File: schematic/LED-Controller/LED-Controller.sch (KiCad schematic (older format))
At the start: 16 parts, among them J1 5V Power, J10 String6, J2 ICSP, J3 RCin, J4 Serial Connect, J5 String1, J6 String2, J7 String3, J8 String4, J9 String5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

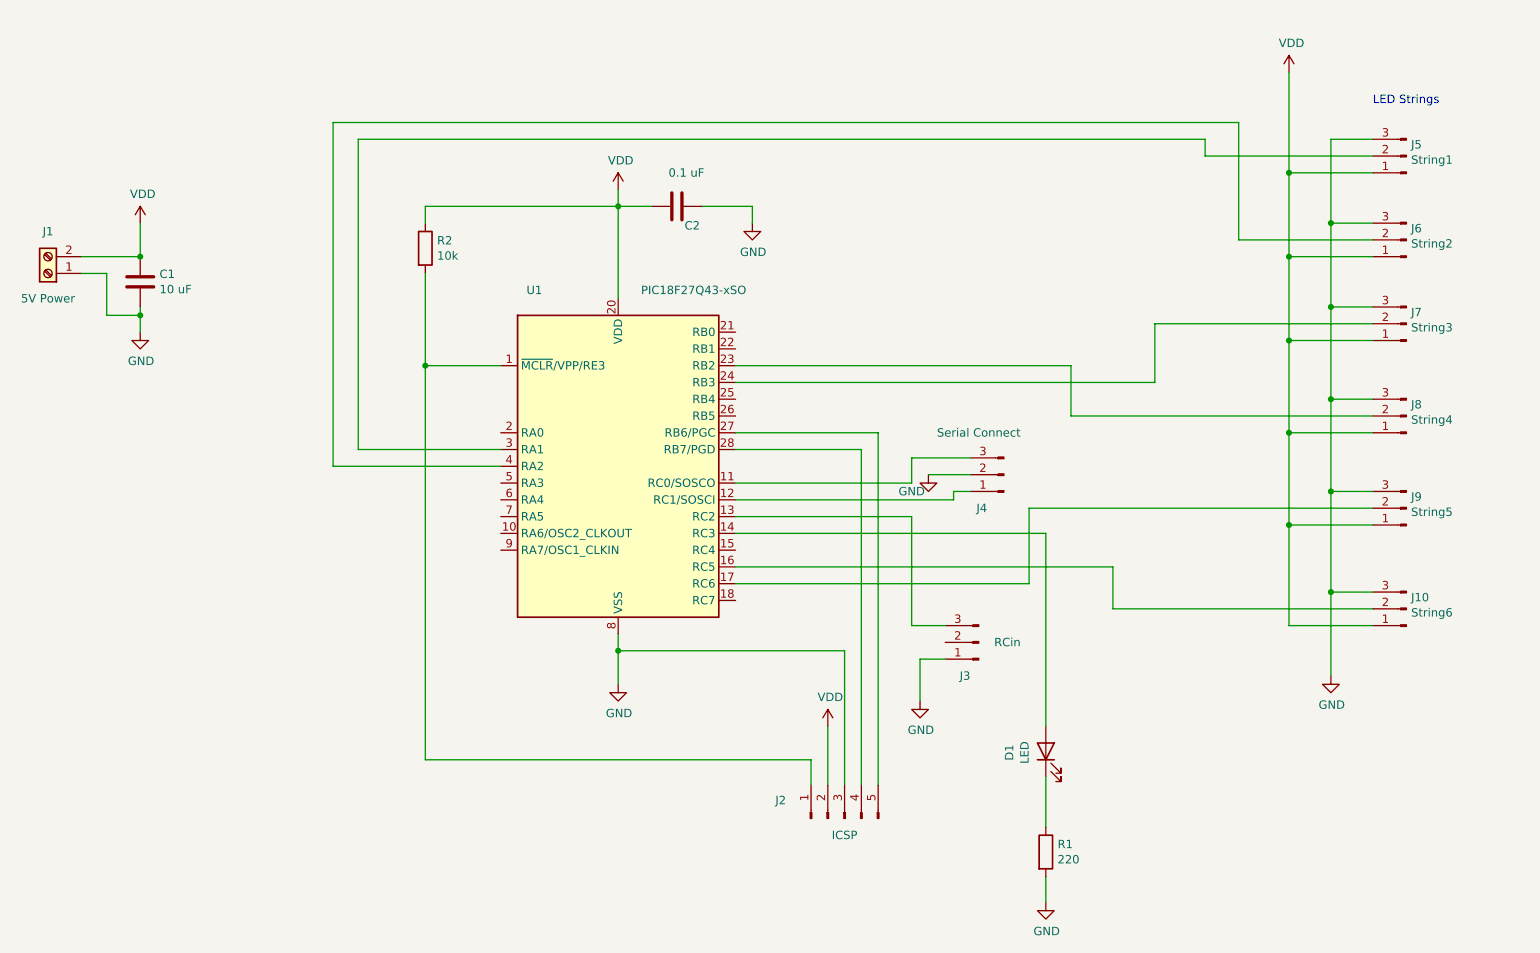
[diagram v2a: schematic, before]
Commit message: Added flexible power for uController
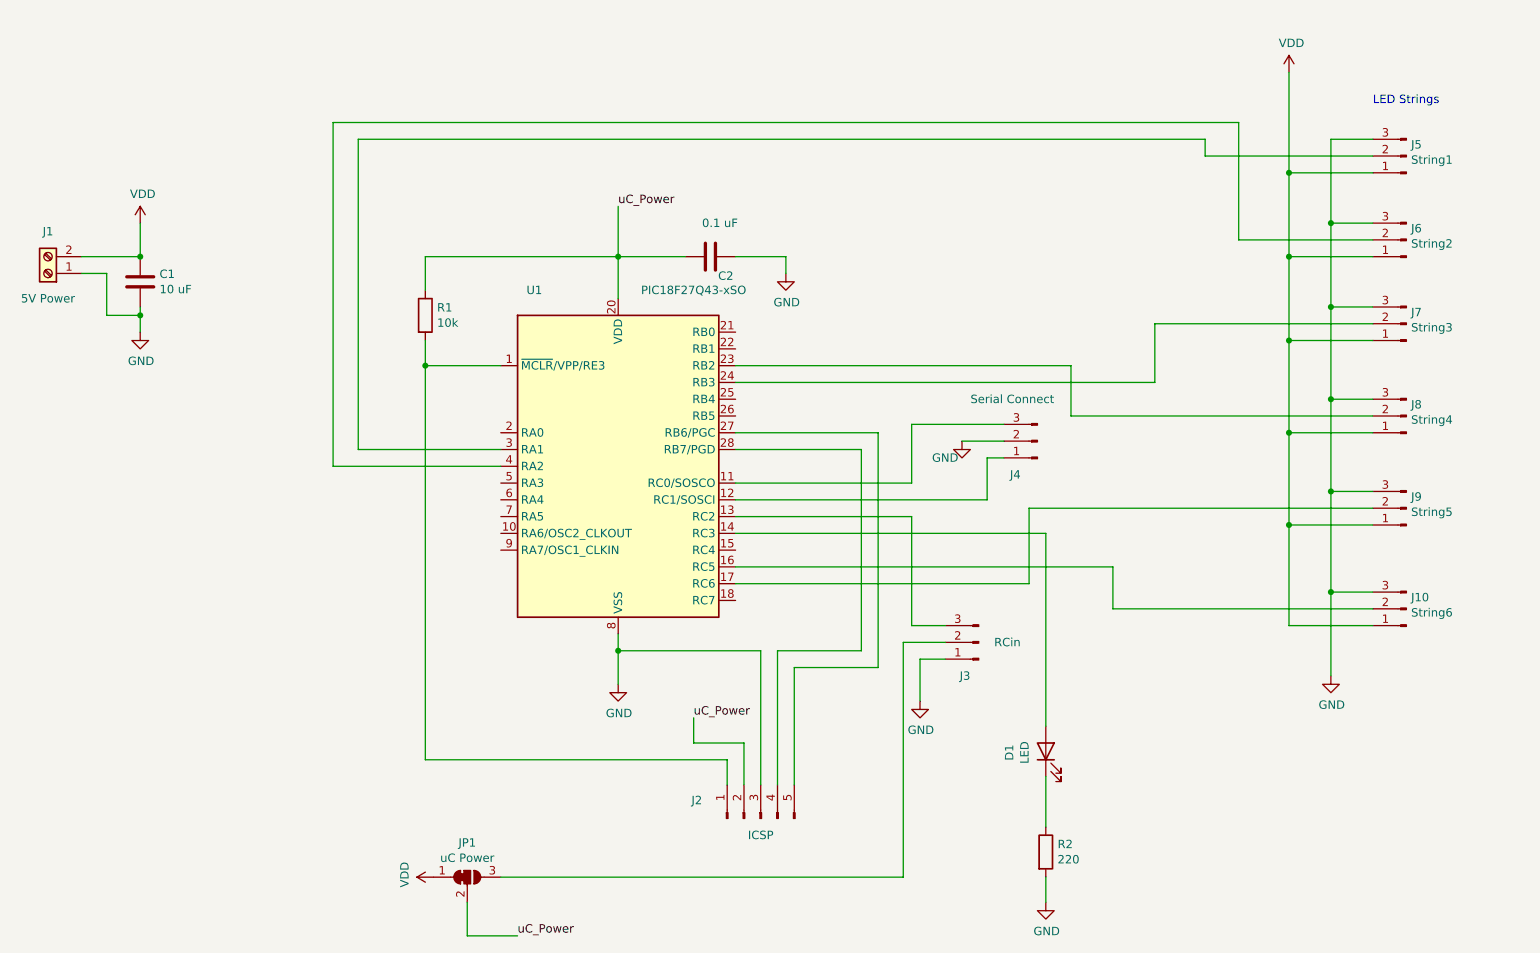
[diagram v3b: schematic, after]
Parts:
- added JP1: uC Power, symbol Jumper:SolderJumper_3_Bridged12
- renumbered R2 to R1, R1 to R2
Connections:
- net VDD: now also JP1.1 (A); no longer C2.2, J2.2 (Pin_2), R1.1, U1.20 (VDD)
- net at J3.2 (Pin_2): now also JP1.3 (B)
- new net uC_Power: C2.2, J2.2 (Pin_2), JP1.2 (C), R1.1, U1.20 (VDD)
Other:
- moved on the sheet: C2, J2, J4, R1
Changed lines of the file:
@@
 L Connector:Conn_01x03_Male J4
 U 1 1 602A7478
-P 6750 3600
-F 0 "J4" H 6850 3800 50  0000 L CNN
-F 1 "Serial Connect" H 6650 3350 50  0000 L CNN
-F 2 "Connector_PinHeader_2.54mm:PinHeader_1x03_P2.54mm_Vertical" H 6750 3600 50  0001 C CNN
-F 3 "~" H 6750 3600 50  0001 C CNN
-	1    6750 3600
+P 6950 3400
+F 0 "J4" H 7050 3600 50  0000 L CNN
+F 1 "Serial Connect" H 6850 3150 50  0000 L CNN
+F 2 "Connector_PinHeader_2.54mm:PinHeader_1x03_P2.54mm_Vertical" H 6950 3400 50  0001 C CNN
+F 3 "~" H 6950 3400 50  0001 C CNN
+	1    6950 3400
 	-1   0    0    1
 $EndComp
@@
 L Device:C C2
 U 1 1 602AFB39
-P 4800 2000
-F 0 "C2" V 4915 2046 50  0000 L CNN
-F 1 "0.1 uF" V 4600 1950 50  0000 L CNN
-F 2 "Capacitor_SMD:C_0603_1608Metric_Pad1.08x0.95mm_HandSolder" H 4838 1850 50  0001 C CNN
-F 3 "~" H 4800 2000 50  0001 C CNN
-	1    4800 2000
+P 5000 2300
+F 0 "C2" V 5115 2346 50  0000 L CNN
+F 1 "0.1 uF" V 4800 2250 50  0000 L CNN
+F 2 "Capacitor_SMD:C_0603_1608Metric_Pad1.08x0.95mm_HandSolder" H 5038 2150 50  0001 C CNN
+F 3 "~" H 5000 2300 50  0001 C CNN
+	1    5000 2300
 	0    1    1    0
 $EndComp
@@
 $EndComp
 $Comp
-L power:GND #PWR06
+L power:GND #PWR05
 U 1 1 602B1183
-P 5250 2100
-F 0 "#PWR06" H 5250 1850 50  0001 C CNN
-F 1 "GND" H 5255 1927 50  0000 C CNN
-F 2 "" H 5250 2100 50  0001 C CNN
-F 3 "" H 5250 2100 50  0001 C CNN
-	1    5250 2100
+P 5450 2400
+F 0 "#PWR05" H 5450 2150 50  0001 C CNN
+F 1 "GND" H 5455 2227 50  0000 C CNN
+F 2 "" H 5450 2400 50  0001 C CNN
+F 3 "" H 5450 2400 50  0001 C CNN
+	1    5450 2400
 	1    0    0    -1
 $EndComp
@@
 $EndComp
 $Comp
-L power:VDD #PWR010
+L power:VDD #PWR09
 U 1 1 602C05A1
 P 8450 1200
-F 0 "#PWR010" H 8450 1050 50  0001 C CNN
+F 0 "#PWR09" H 8450 1050 50  0001 C CNN
 F 1 "VDD" H 8465 1373 50  0000 C CNN
 F 2 "" H 8450 1200 50  0001 C CNN
@@
 $EndComp
 $Comp
-L power:GND #PWR011
+L power:GND #PWR010
 U 1 1 602C0B28
 P 8700 4800
-F 0 "#PWR011" H 8700 4550 50  0001 C CNN
+F 0 "#PWR010" H 8700 4550 50  0001 C CNN
 F 1 "GND" H 8705 4627 50  0000 C CNN
 F 2 "" H 8700 4800 50  0001 C CNN
@@
 L Connector:Conn_01x05_Male J2
 U 1 1 602D318D
-P 5800 5650
-F 0 "J2" V 5908 6031 50  0000 C CNN
-F 1 "ICSP" V 5700 5650 50  0000 C CNN
-F 2 "Connector_PinHeader_2.54mm:PinHeader_1x05_P2.54mm_Vertical" H 5800 5650 50  0001 C CNN
-F 3 "~" H 5800 5650 50  0001 C CNN
-	1    5800 5650
+P 5300 5650
+F 0 "J2" V 5408 6031 50  0000 C CNN
+F 1 "ICSP" V 5200 5650 50  0000 C CNN
+F 2 "Connector_PinHeader_2.54mm:PinHeader_1x05_P2.54mm_Vertical" H 5300 5650 50  0001 C CNN
+F 3 "~" H 5300 5650 50  0001 C CNN
+	1    5300 5650
 	0    -1   -1   0
 $EndComp
@@
 $EndComp
 $Comp
-L Device:R R2
+L Device:R R1
 U 1 1 6029F916
-P 3300 2250
-F 0 "R2" H 3370 2296 50  0000 L CNN
-F 1 "10k" H 3370 2205 50  0000 L CNN
-F 2 "Resistor_SMD:R_0603_1608Metric" V 3230 2250 50  0001 C CNN
-F 3 "~" H 3300 2250 50  0001 C CNN
-	1    3300 2250
+P 3300 2650
+F 0 "R1" H 3370 2696 50  0000 L CNN
+F 1 "10k" H 3370 2605 50  0000 L CNN
+F 2 "Resistor_SMD:R_0603_1608Metric" V 3230 2650 50  0001 C CNN
+F 3 "~" H 3300 2650 50  0001 C CNN
+	1    3300 2650
 	1    0    0    -1
 $EndComp
@@
 	3750 2950 3300 2950
 Wire Wire Line
-	3300 2950 3300 2400
-$Comp
-L power:VDD #PWR04
+	3300 2950 3300 2800
+$Comp
+L power:VDD #PWR03
 U 1 1 602A05DD
-P 4450 1900
-F 0 "#PWR04" H 4450 1750 50  0001 C CNN
-F 1 "VDD" H 4465 2073 50  0000 C CNN
-F 2 "" H 4450 1900 50  0001 C CNN
-F 3 "" H 4450 1900 50  0001 C CNN
-	1    4450 1900
-	1    0    0    -1
-$EndComp
-Wire Wire Line
-	3300 2100 3300 2000
-Wire Wire Line
-	3300 2000 4450 2000
-Wire Wire Line
-	4450 1900 4450 2000
-Connection ~ 4450 2000
-Wire Wire Line
-	4450 2000 4450 2550
-$Comp
-L power:GND #PWR05
+P 3350 6000
+F 0 "#PWR03" H 3350 5850 50  0001 C CNN
+F 1 "VDD" H 3365 6173 50  0000 C CNN
+F 2 "" H 3350 6000 50  0001 C CNN
+F 3 "" H 3350 6000 50  0001 C CNN
+	1    3350 6000
+	0    -1   -1   0
+$EndComp
+Wire Wire Line
+	3300 2300 4450 2300
+$Comp
+L power:GND #PWR04
 U 1 1 602A2E68
 P 4450 4850
-F 0 "#PWR05" H 4450 4600 50  0001 C CNN
+F 0 "#PWR04" H 4450 4600 50  0001 C CNN
 F 1 "GND" H 4455 4677 50  0000 C CNN
 F 2 "" H 4450 4850 50  0001 C CNN
@@
 	4450 4850 4450 4650
 Wire Wire Line
-	5250 2100 5250 2000
-Wire Wire Line
-	5250 2000 4950 2000
-Wire Wire Line
-	4650 2000 4450 2000
+	5450 2400 5450 2300
+Wire Wire Line
+	5450 2300 5150 2300
 Wire Wire Line
 	3300 2950 3300 5300
-Wire Wire Line
-	3300 5300 5600 5300
-Wire Wire Line
-	5600 5300 5600 5450
 Connection ~ 3300 2950
-Wire Wire Line
-	5800 5450 5800 4650
-Wire Wire Line
-	5800 4650 4450 4650
 Connection ~ 4450 4650
 Wire Wire Line
 	4450 4650 4450 4550
-$Comp
-L power:VDD #PWR07
-U 1 1 602AD71B
-P 5700 5100
-F 0 "#PWR07" H 5700 4950 50  0001 C CNN
-F 1 "VDD" H 5715 5273 50  0000 C CNN
-F 2 "" H 5700 5100 50  0001 C CNN
-F 3 "" H 5700 5100 50  0001 C CNN
-	1    5700 5100
-	1    0    0    -1
-$EndComp
-Wire Wire Line
-	5700 5450 5700 5100
 Wire Wire Line
 	5150 3450 5900 3450
 Wire Wire Line
-	5900 3450 5900 5450
+	5900 3450 5900 4650
 Wire Wire Line
 	5150 3350 6000 3350
 Wire Wire Line
-	6000 3350 6000 5450
-Wire Wire Line
 	3750 3450 2900 3450
 Wire Wire Line
@@
 	7150 3250 8950 3250
 Wire Wire Line
-	5150 3750 6450 3750
-Wire Wire Line
-	6450 3750 6450 3700
-Wire Wire Line
-	6450 3700 6550 3700
+	6650 3500 6750 3500
 Wire Wire Line
 	5150 3650 6200 3650
-Wire Wire Line
-	6200 3650 6200 3500
-Wire Wire Line
-	6200 3500 6550 3500
-$Comp
-L power:GND #PWR09
+$Comp
+L power:GND #PWR07
 U 1 1 602BC9A3
-P 6300 3600
-F 0 "#PWR09" H 6300 3350 50  0001 C CNN
-F 1 "GND" H 6200 3500 50  0000 C CNN
-F 2 "" H 6300 3600 50  0001 C CNN
-F 3 "" H 6300 3600 50  0001 C CNN
-	1    6300 3600
-	1    0    0    -1
-$EndComp
-Wire Wire Line
-	6550 3600 6300 3600
+P 6500 3400
+F 0 "#PWR07" H 6500 3150 50  0001 C CNN
+F 1 "GND" H 6400 3300 50  0000 C CNN
+F 2 "" H 6500 3400 50  0001 C CNN
+F 3 "" H 6500 3400 50  0001 C CNN
+	1    6500 3400
+	1    0    0    -1
+$EndComp
+Wire Wire Line
+	6750 3400 6500 3400
 Wire Wire Line
 	5150 3850 6200 3850
@@
 	6200 4500 6400 4500
 $Comp
-L power:GND #PWR08
+L power:GND #PWR06
 U 1 1 602C1BEB
 P 6250 4950
-F 0 "#PWR08" H 6250 4700 50  0001 C CNN
+F 0 "#PWR06" H 6250 4700 50  0001 C CNN
 F 1 "GND" H 6255 4777 50  0000 C CNN
 F 2 "" H 6250 4950 50  0001 C CNN
@@
 $EndComp
 $Comp
-L Device:R R1
+L Device:R R2
 U 1 1 602B7BC0
 P 7000 5850
-F 0 "R1" H 7070 5896 50  0000 L CNN
+F 0 "R2" H 7070 5896 50  0000 L CNN
 F 1 "220" H 7070 5805 50  0000 L CNN
 F 2 "Resistor_SMD:R_0603_1608Metric" V 6930 5850 50  0001 C CNN
@@
 $EndComp
 $Comp
-L power:GND #PWR03
+L power:GND #PWR08
 U 1 1 602B7F4F
 P 7000 6150
-F 0 "#PWR03" H 7000 5900 50  0001 C CNN
+F 0 "#PWR08" H 7000 5900 50  0001 C CNN
 F 1 "GND" H 7005 5977 50  0000 C CNN
 F 2 "" H 7000 6150 50  0001 C CNN
@@
 Wire Wire Line
 	7000 5400 7000 5700
+$Comp
+L Jumper:SolderJumper_3_Bridged12 JP1
+U 1 1 602C7A81
+P 3550 6000
+F 0 "JP1" H 3550 6205 50  0000 C CNN
+F 1 "uC Power" H 3550 6114 50  0000 C CNN
+F 2 "" H 3550 6000 50  0001 C CNN
+F 3 "~" H 3550 6000 50  0001 C CNN
+	1    3550 6000
+	1    0    0    -1
+$EndComp
+Connection ~ 4450 2300
+Wire Wire Line
+	4450 2300 4450 2550
+Wire Wire Line
+	3300 2300 3300 2500
+Wire Wire Line
+	4450 2300 4850 2300
+Wire Wire Line
+	6650 3750 6650 3500
+Wire Wire Line
+	6200 3300 6200 3650
+Wire Wire Line
+	6200 3300 6750 3300
+Wire Wire Line
+	5150 3750 6650 3750
+Text Label 4450 2000 0    50   ~ 0
+uC_Power
+Wire Wire Line
+	4450 2300 4450 2000
+Wire Wire Line
+	6150 6000 6150 4600
+Wire Wire Line
+	6150 4600 6400 4600
+Wire Wire Line
+	3750 6000 6150 6000
+Wire Wire Line
+	5100 5450 5100 5300
+Wire Wire Line
+	5100 5300 3300 5300
+Wire Wire Line
+	5300 5450 5300 4650
+Wire Wire Line
+	5300 4650 4450 4650
+Wire Wire Line
+	5400 5450 5400 4650
+Wire Wire Line
+	5400 4650 5900 4650
+Wire Wire Line
+	5500 5450 5500 4750
+Wire Wire Line
+	5500 4750 6000 4750
+Wire Wire Line
+	6000 3350 6000 4750
+Text Label 4900 5050 0    50   ~ 0
+uC_Power
+Wire Wire Line
+	5200 5450 5200 5200
+Wire Wire Line
+	5200 5200 4900 5200
+Wire Wire Line
+	4900 5200 4900 5050
+Text Label 3850 6350 0    50   ~ 0
+uC_Power
+Wire Wire Line
+	3550 6350 3850 6350
+Wire Wire Line
+	3550 6150 3550 6350
 $EndSCHEMATC

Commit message: Changed connectors
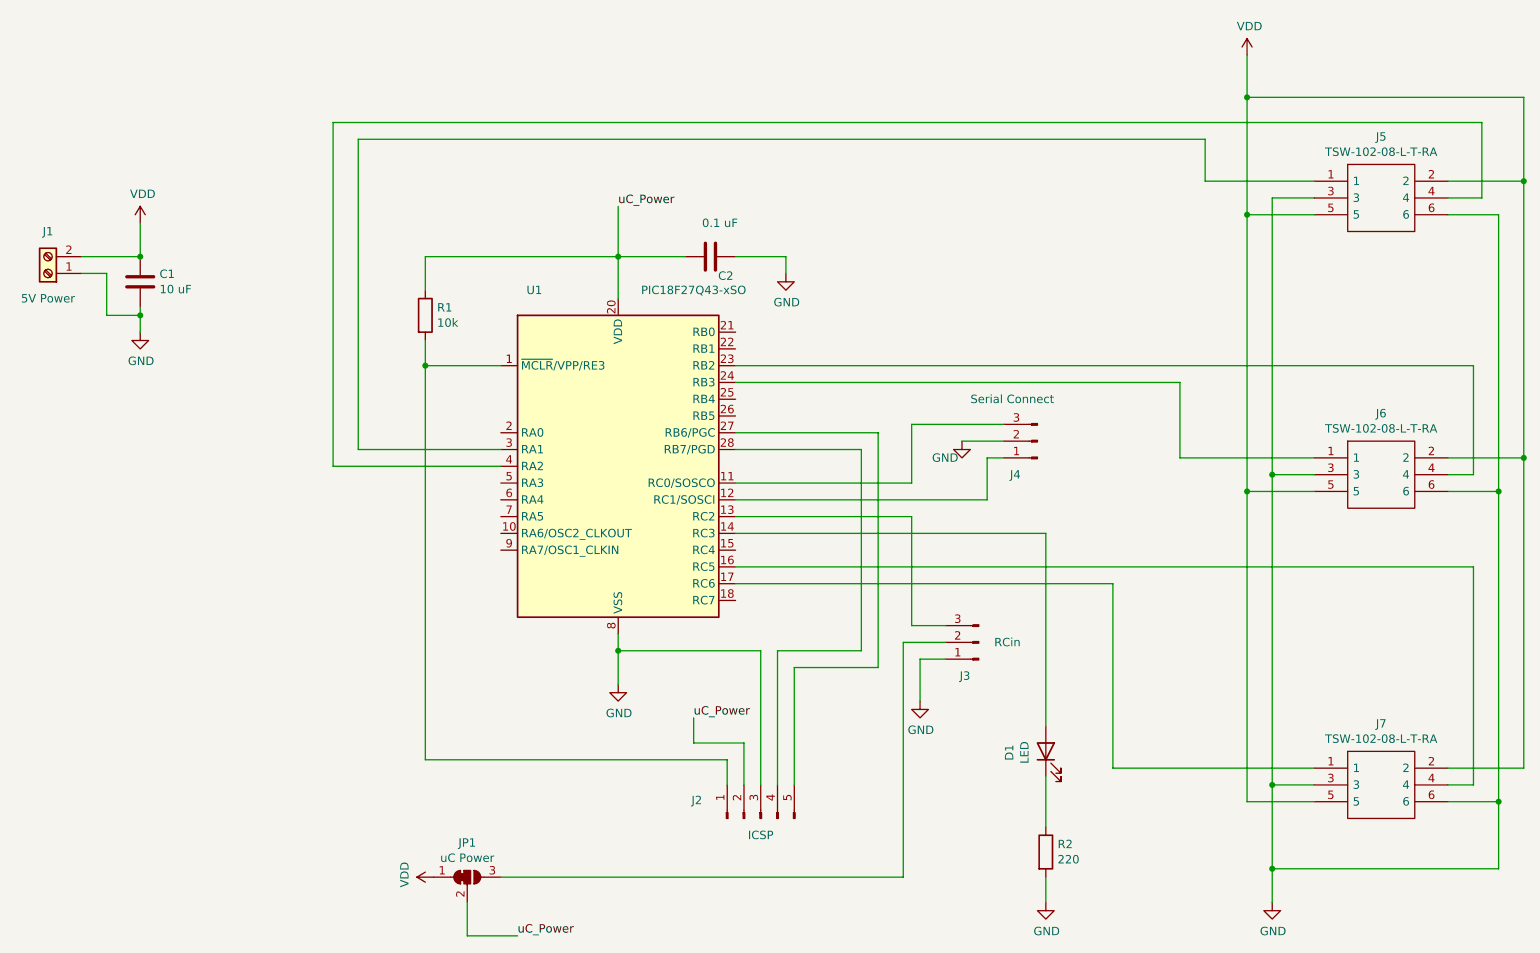
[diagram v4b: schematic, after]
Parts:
- removed J10: String6, LEDStringConn:TopBottom_3Pin, symbol Connector:Conn_01x03_Male
- removed J5: String1, LEDStringConn:TopBottom_3Pin, symbol Connector:Conn_01x03_Male
- removed J6: String2, LEDStringConn:TopBottom_3Pin, symbol Connector:Conn_01x03_Male
- removed J7: String3, LEDStringConn:TopBottom_3Pin, symbol Connector:Conn_01x03_Male
- removed J8: String4, LEDStringConn:TopBottom_3Pin, symbol Connector:Conn_01x03_Male
- removed J9: String5, LEDStringConn:TopBottom_3Pin, symbol Connector:Conn_01x03_Male
- added J5, J6, J7: TSW-102-08-L-T-RA, HDRRA6W64P254_3X2_508X254X810P, symbol SamacSys_Parts:TSW-102-08-L-T-RA
- J1: footprint Connector_Wire:SolderWire-2.5sqmm_1x02_P8.8mm_D2.4mm_OD4.4mm -> Connector_Wire:SolderWire-1sqmm_1x02_P5.4mm_D1.4mm_OD2.7mm
- JP1: footprint (none) -> Jumper:SolderJumper-3_P1.3mm_Bridged12_RoundedPad1.0x1.5mm_NumberLabels
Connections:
- net GND: now also J5.3, J5.6, J6.3, J6.6, J7.3, J7.6
- net VDD: now also J5.2, J5.5, J6.2, J6.5, J7.2, J7.5
- net at U1.3 (RA1): now also J5.1
- net at U1.4 (RA2): now also J5.4
- net at U1.24 (RB3): now also J6.1
- net at U1.23 (RB2): now also J6.4
- net at U1.17 (RC6): now also J7.1
- net at U1.16 (RC5): now also J7.4
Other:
- note removed: "LED Strings"
